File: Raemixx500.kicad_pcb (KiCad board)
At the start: 2 copper layers, 365.8 x 254 mm, 372 parts, among them CN1 LEFT_JOY, CN10 COMPOSITE, CN11 INTERNAL_FLOPPY, CN12 FLOPPY_POWER, CN13 KEYBOARD, CN14 IDE_POWER, CN15 IDE_I/F, CN2 RIGHT_JOY, CN3 RIGHT, CN4 LEFT, CN5 EXTFLOPPY_DB23F, CN6 SERIAL_DB25M, CN7 PARALLEL_DB25F, CN8 POWER, CN9 VIDEO_DB23M, J90 DRIVE_SWITCHER, J91 Dispatcher_3to1, J92 Dispatcher_3to1, J93 Dispatcher_3to1, J99 CONN_HDACT, P1 EXPANSION BUS, P9 TRAPDOOR, Q301 2N3906, Q321 MPF102, Q331 MPF102, Q501 2N3904, Q502 2N3906, Q503 2N3906, Q711 2N3904, Q921 MMBFJ113, Q931 MMBFJ113, Q99 2N3906, U1 68000D, U10 74LS244, U11 74LS373, U12 74LS244, U13 74LS373, U14 LF347, U15 74LS157, U16 SIMM, U17 74LS08, U18 74LS74, U19 74F00, U2 FAT_AGNUS_8375, U3 PAULA, U32 74LS139, U33 74LS258, U34 74LS244, U35 74LS244, U36 74LS05, U37 74LS32, U38 MC1488, U39 MC1489, U4 DENISE, U40 74LS245, U41 74LS245, U42 NE555, U5 GARY_5719, U6 ROM, U7 VIA_8520, U8 VIA_8520, U9 MSM6242B, U90 DT1042, U91 DT1042, U92 DT1042, U93 DT1042, U94 74HCT14, X1 XTAL, Y9 32768

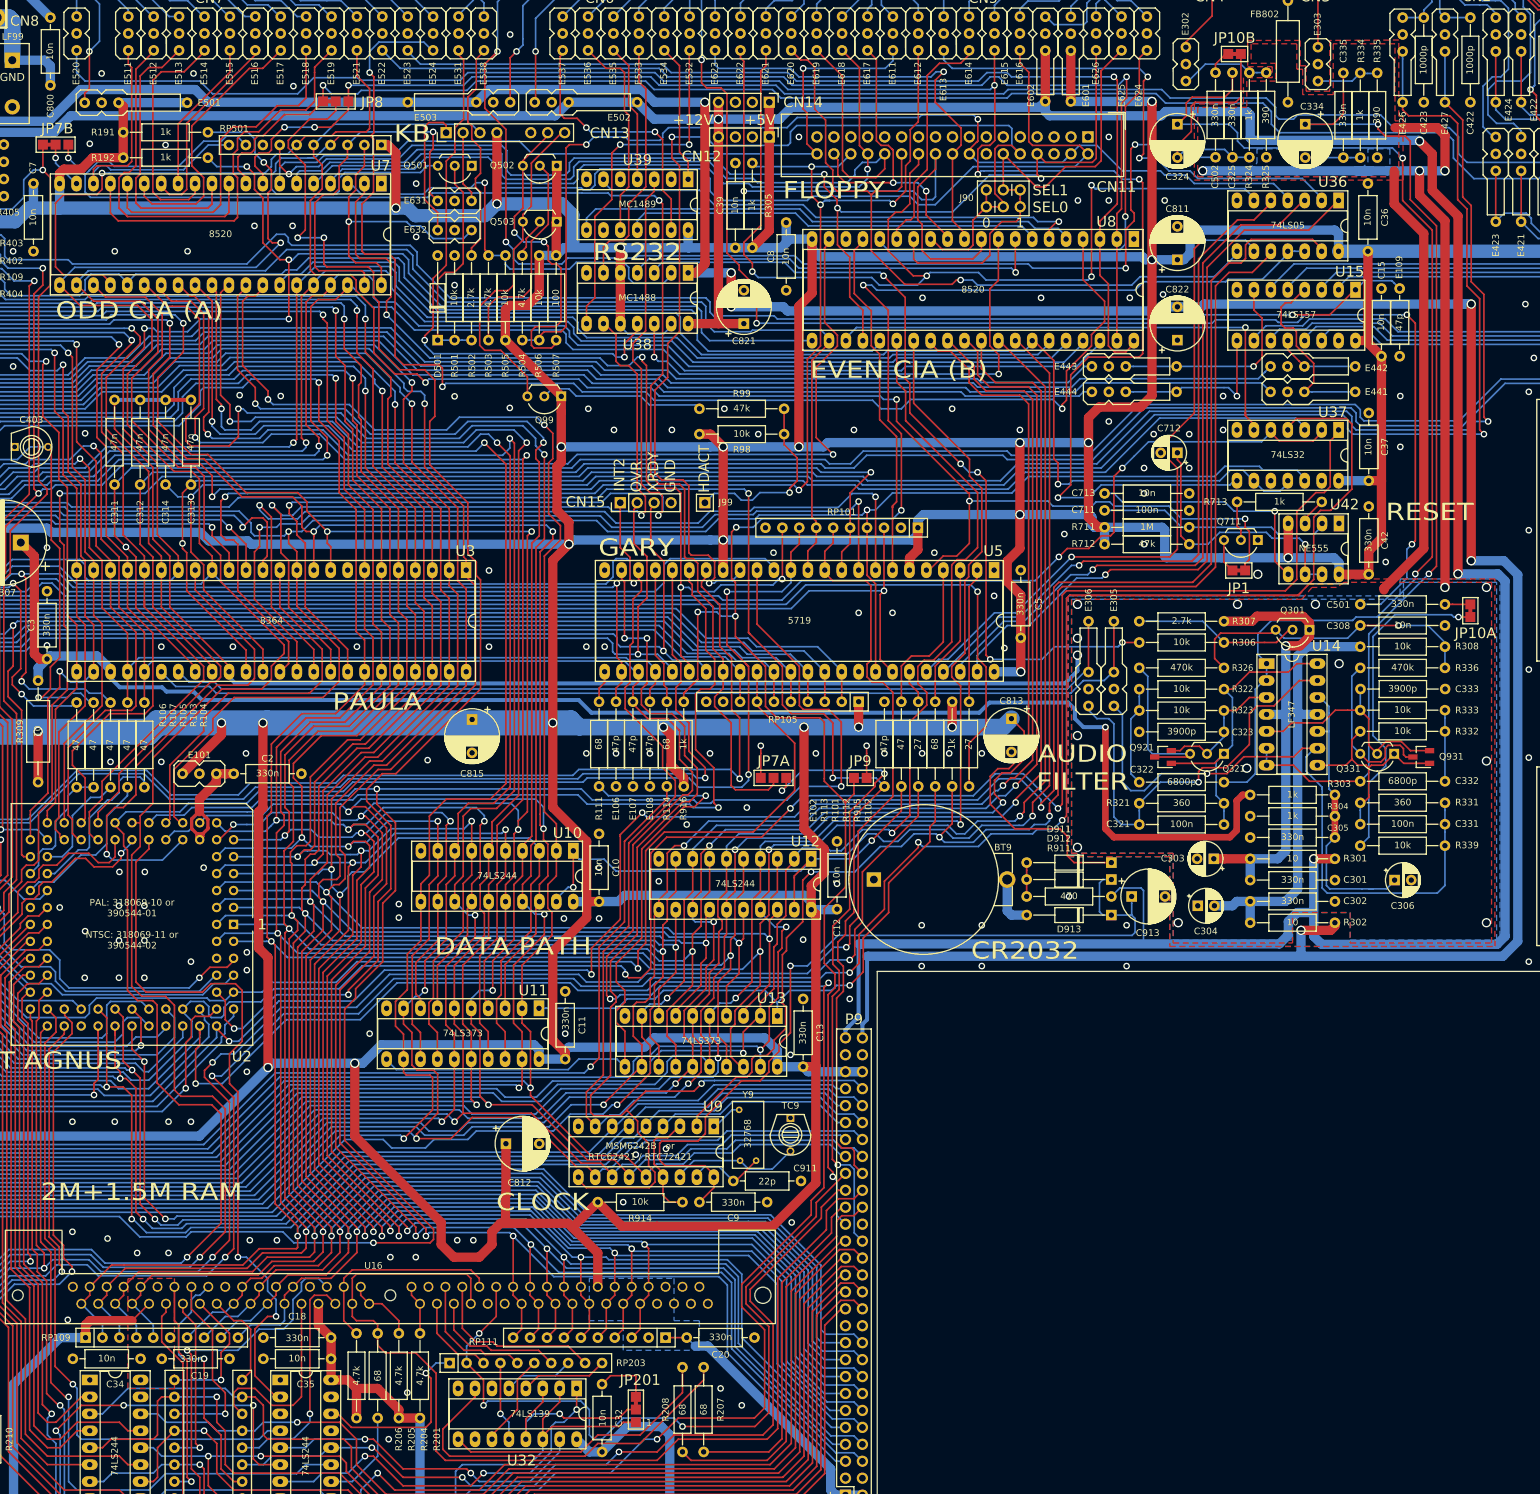
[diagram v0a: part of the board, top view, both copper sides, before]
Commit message: removed some unnecessary copper zones
improved grounding around SIMM a bit
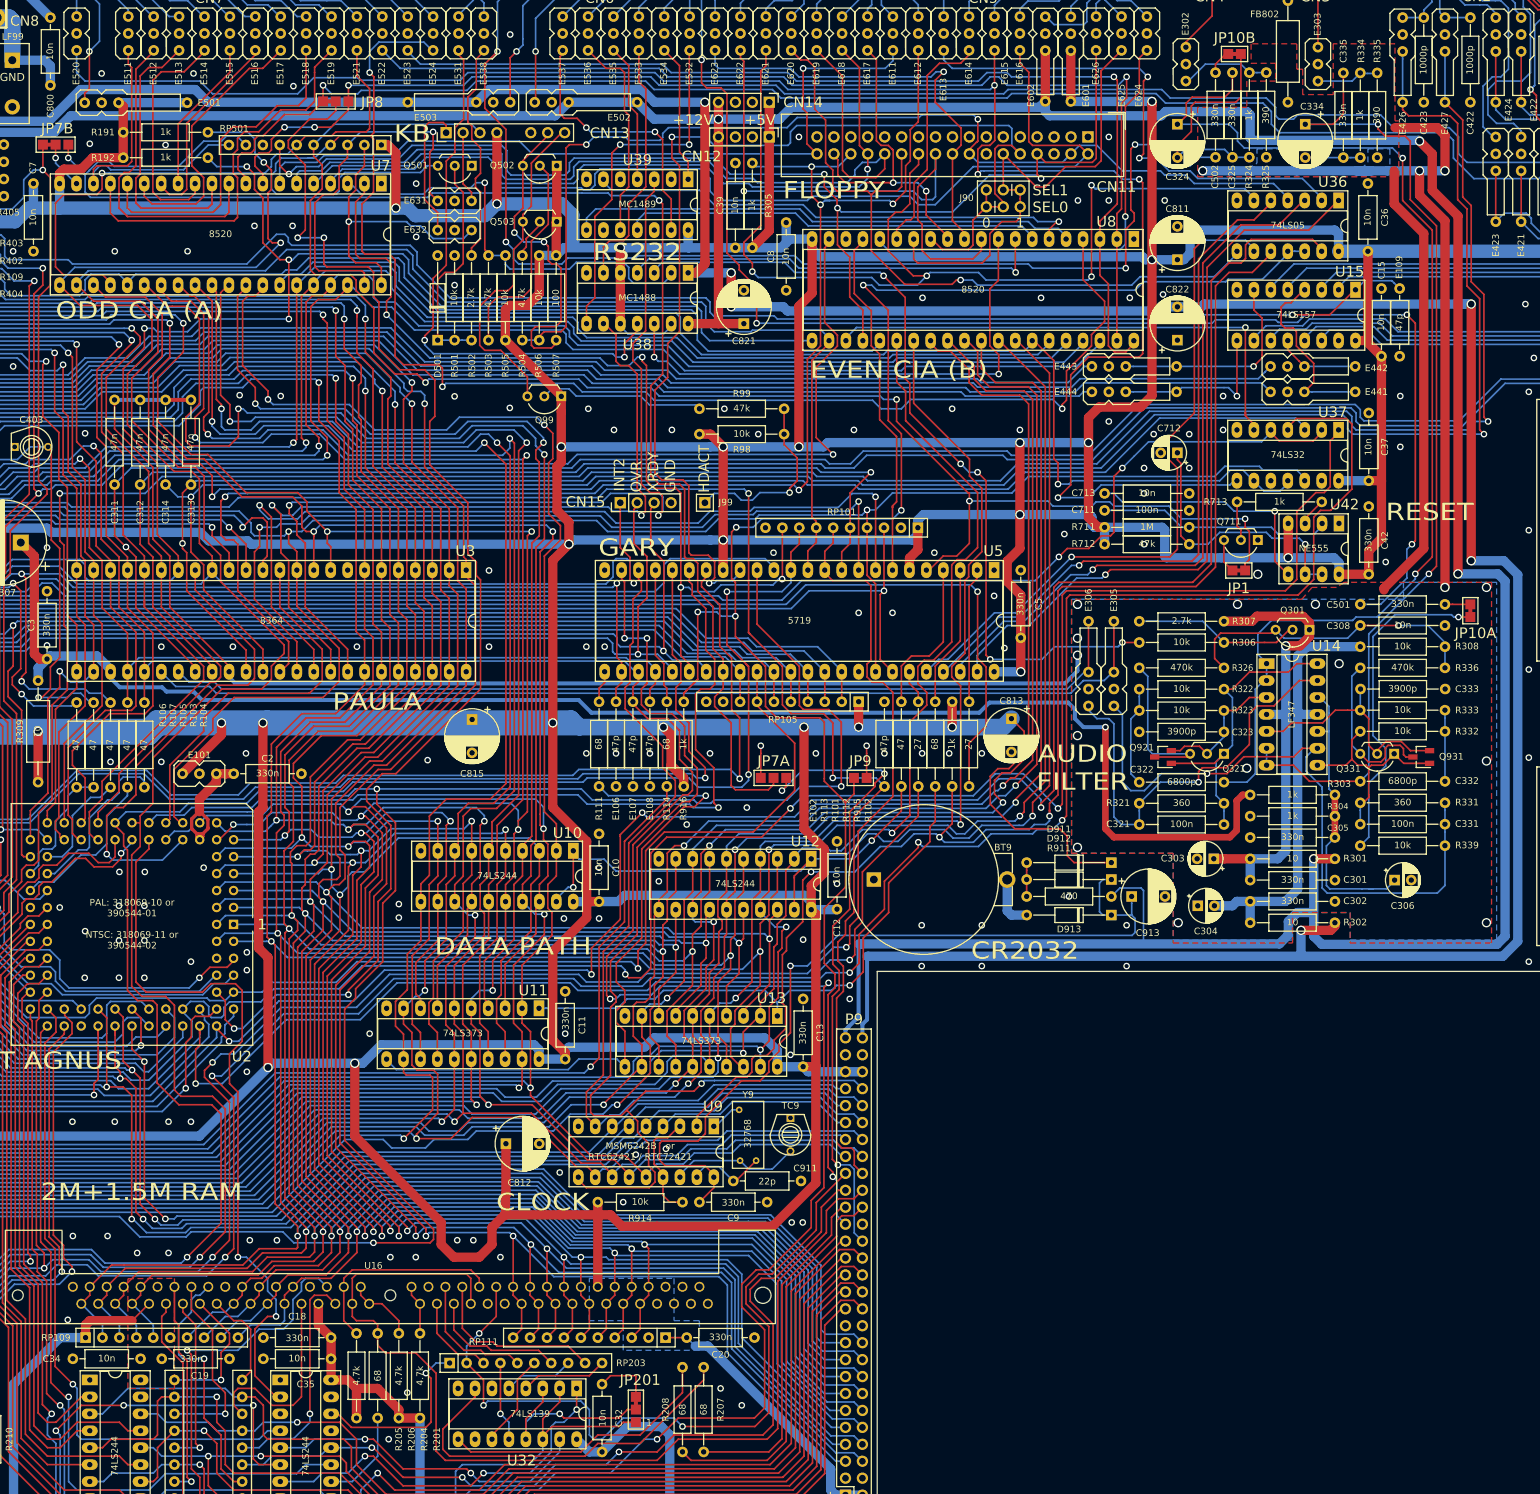
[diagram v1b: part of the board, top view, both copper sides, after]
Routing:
- net ~{BWE}: track 114.5 -> 115.7 mm
- net BDRA9: track 130.0 -> 131.2 mm
- net CCKQ: track 505.4 -> 506.5 mm
- net VCC: track 3035.7 -> 3034.9 mm
- net GND: vias 281 -> 284
